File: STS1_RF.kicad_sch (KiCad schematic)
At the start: 84 parts, among them J1 UHF, Q1 SQ2318, Q3 SQ2318, Q4 SQ2318, U10 TQP3M9036, U11 NL17SV04XV5T2G, U16 F2972, U2 LP2985-1.8, U30 TMP36xS, U4 74LVC2G74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

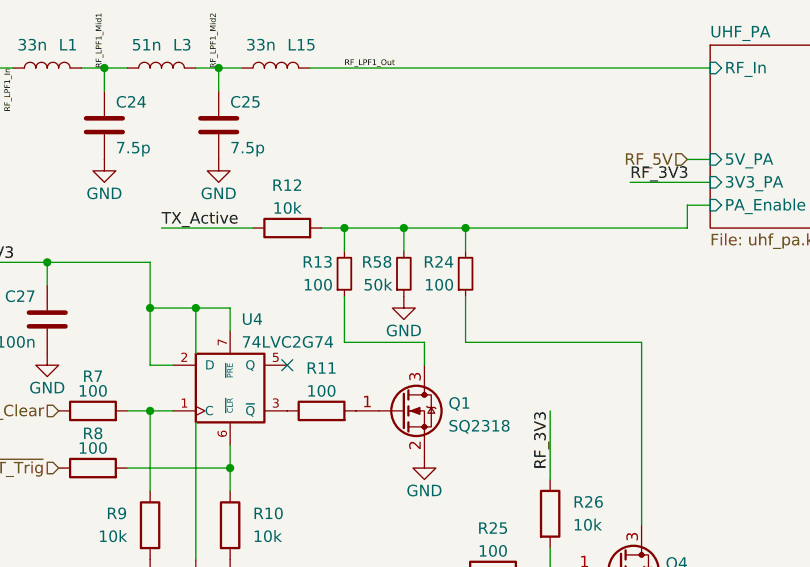
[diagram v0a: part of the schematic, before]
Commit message: Add a pull-up resistor for FLT pin of U12 and decouple U12 and STM with a series resistor
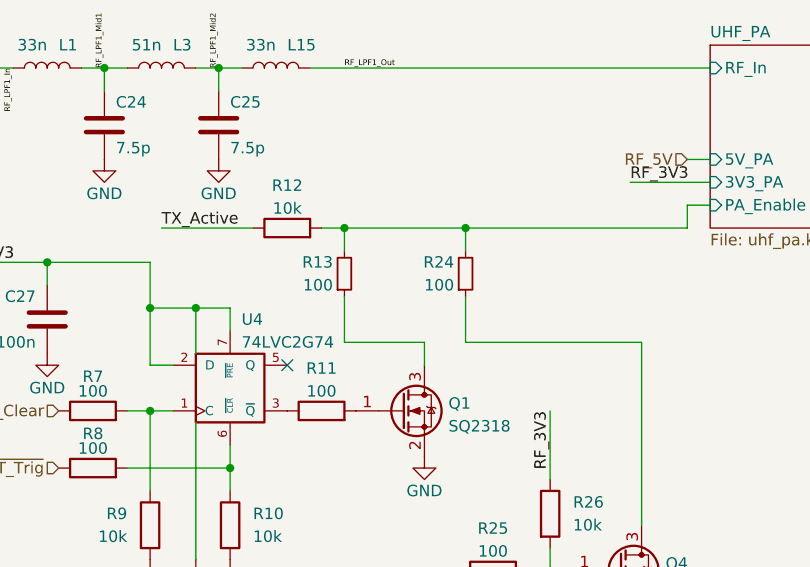
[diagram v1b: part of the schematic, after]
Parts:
- removed R58: 50k, Resistor_SMD:R_0603_1608Metric, symbol Device:R_Small
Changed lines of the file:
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@@
   (junction (at 152.4 50.8) (diameter 0) (color 0 0 0 0)
   )
-  (junction (at 67.564 116.84) (diameter 0) (color 0 0 0 0)
-  )
   (junction (at 48.26 143.51) (diameter 0) (color 0 0 0 0)
   )
@@
     (stroke (width 0) (type default) (color 0 0 0 0))
   )
-  (wire (pts (xy 67.564 116.84) (xy 74.422 116.84))
-    (stroke (width 0) (type default) (color 0 0 0 0))
-  )
   (wire (pts (xy 100.33 55.88) (xy 120.65 55.88))
     (stroke (width 0) (type default) (color 0 0 0 0))
@@
     (stroke (width 0) (type default) (color 0 0 0 0))
   )
-  (wire (pts (xy 67.564 116.84) (xy 67.564 119.38))
-    (stroke (width 0) (type default) (color 0 0 0 0))
-  )
   (wire (pts (xy 165.1 21.59) (xy 172.72 21.59))
     (stroke (width 0) (type default) (color 0 0 0 0))
@@
     (stroke (width 0) (type default) (color 0 0 0 0))
   )
-  (wire (pts (xy 60.96 116.84) (xy 67.564 116.84))
+  (wire (pts (xy 60.96 116.84) (xy 74.422 116.84))
     (stroke (width 0) (type default) (color 0 0 0 0))
   )
@@
     (pin "2")
   )
-  (symbol (lib_id "Device:R_Small") (at 67.564 121.92 0) (mirror x) (unit 1)
-    (in_bom yes) (on_board yes)
-    (property "Reference" "R58" (id 0) (at 66.294 120.65 0)
-      (effects (font (size 1.27 1.27)) (justify right))
-    )
-    (property "Value" "50k" (id 1) (at 66.294 123.19 0)
-      (effects (font (size 1.27 1.27)) (justify right))
-    )
-    (property "Footprint" "Resistor_SMD:R_0603_1608Metric" (id 2) (at 67.564 121.92 0)
-      (effects (font (size 1.27 1.27)) hide)
-    )
-    (property "Datasheet" "~" (id 3) (at 67.564 121.92 0)
-      (effects (font (size 1.27 1.27)) hide)
-    )
-    (property "Description" "" (id 4) (at 67.564 121.92 0)
-      (effects (font (size 1.27 1.27)) hide)
-    )
-    (property "Mnf." "" (id 5) (at 67.564 121.92 0)
-      (effects (font (size 1.27 1.27)) hide)
-    )
-    (property "PartNumber" "" (id 6) (at 67.564 121.92 0)
-      (effects (font (size 1.27 1.27)) hide)
-    )
-    (pin "1")
-    (pin "2")
-  )
   (symbol (lib_id "power:GND") (at 227.33 146.05 0) (unit 1)
     (in_bom yes) (on_board yes)
@@
     (pin "2")
   )
-  (symbol (lib_id "power:GND") (at 67.564 124.46 0) (unit 1)
-    (in_bom yes) (on_board yes)
-    (property "Reference" "#PWR058" (id 0) (at 67.564 130.81 0)
-      (effects (font (size 1.27 1.27)) hide)
-    )
-    (property "Value" "GND" (id 1) (at 67.564 128.27 0))
-    (property "Footprint" "" (id 2) (at 67.564 124.46 0)
-      (effects (font (size 1.27 1.27)) hide)
-    )
-    (property "Datasheet" "" (id 3) (at 67.564 124.46 0)
-      (effects (font (size 1.27 1.27)) hide)
-    )
-    (pin "1")
-  )
   (symbol (lib_id "power:GND") (at 27.94 130.81 0) (unit 1)

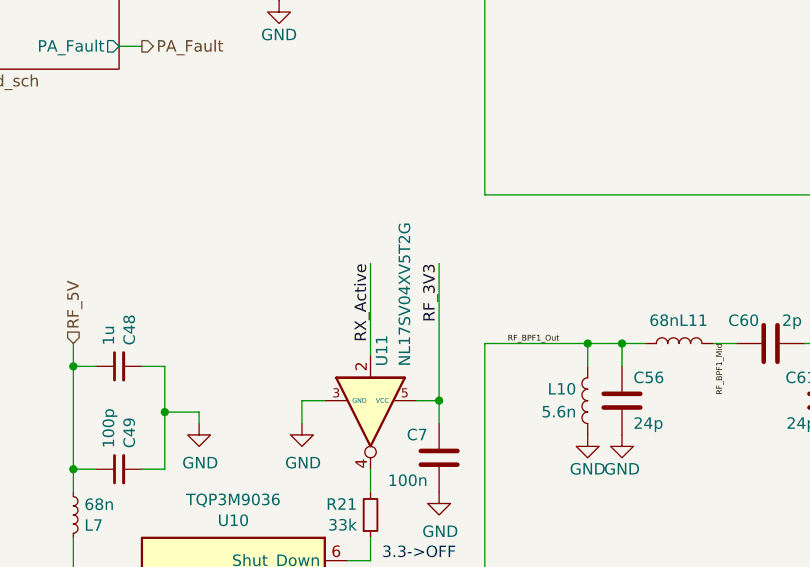
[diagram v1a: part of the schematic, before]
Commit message: Replace U11 NL17SV04XV5T2G with 74LVC1G14Z-7 and add MFT number for R31
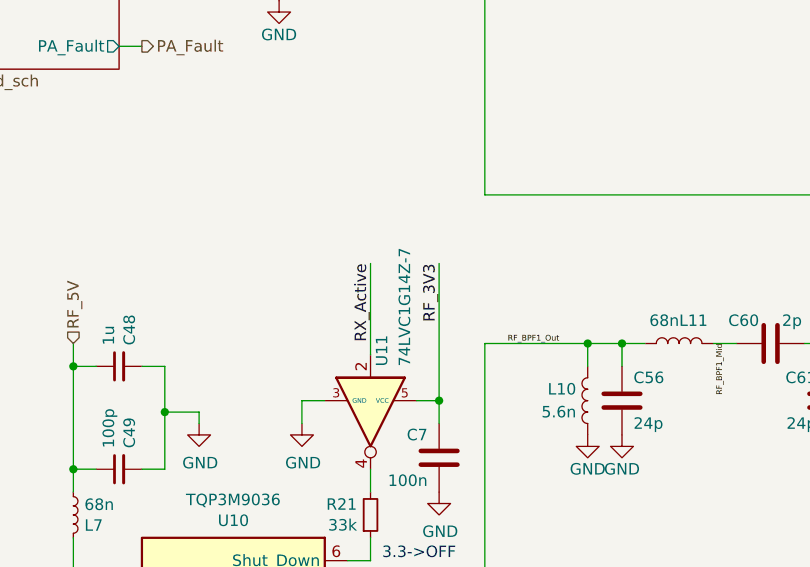
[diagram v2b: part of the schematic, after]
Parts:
- U11: value NL17SV04XV5T2G -> 74LVC1G14Z-7; JLCPCB Part # C185507 -> C3272831; Manufacturer_Part_Number NL17SV04XV5T2G -> 74LVC1G14Z-7
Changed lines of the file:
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@@
       (effects (font (size 1.27 1.27)) (justify right))
     )
-    (property "Value" "NL17SV04XV5T2G" (id 1) (at 161.29 149.86 0)
+    (property "Value" "74LVC1G14Z-7" (id 1) (at 161.29 149.86 0)
       (effects (font (size 1.27 1.27)) (justify right))
     )
@@
       (effects (font (size 1.27 1.27)) hide)
     )
-    (property "Manufacturer_Part_Number" "NL17SV04XV5T2G " (id 6) (at 157.48 153.67 0)
+    (property "Manufacturer_Part_Number" "74LVC1G14Z-7" (id 6) (at 157.48 153.67 0)
       (effects (font (size 1.27 1.27)) hide)
     )
-    (property "JLCPCB Part #" "C185507" (id 7) (at 157.48 153.67 0)
+    (property "JLCPCB Part #" "C3272831" (id 7) (at 157.48 153.67 0)
       (effects (font (size 1.27 1.27)) hide)
     )

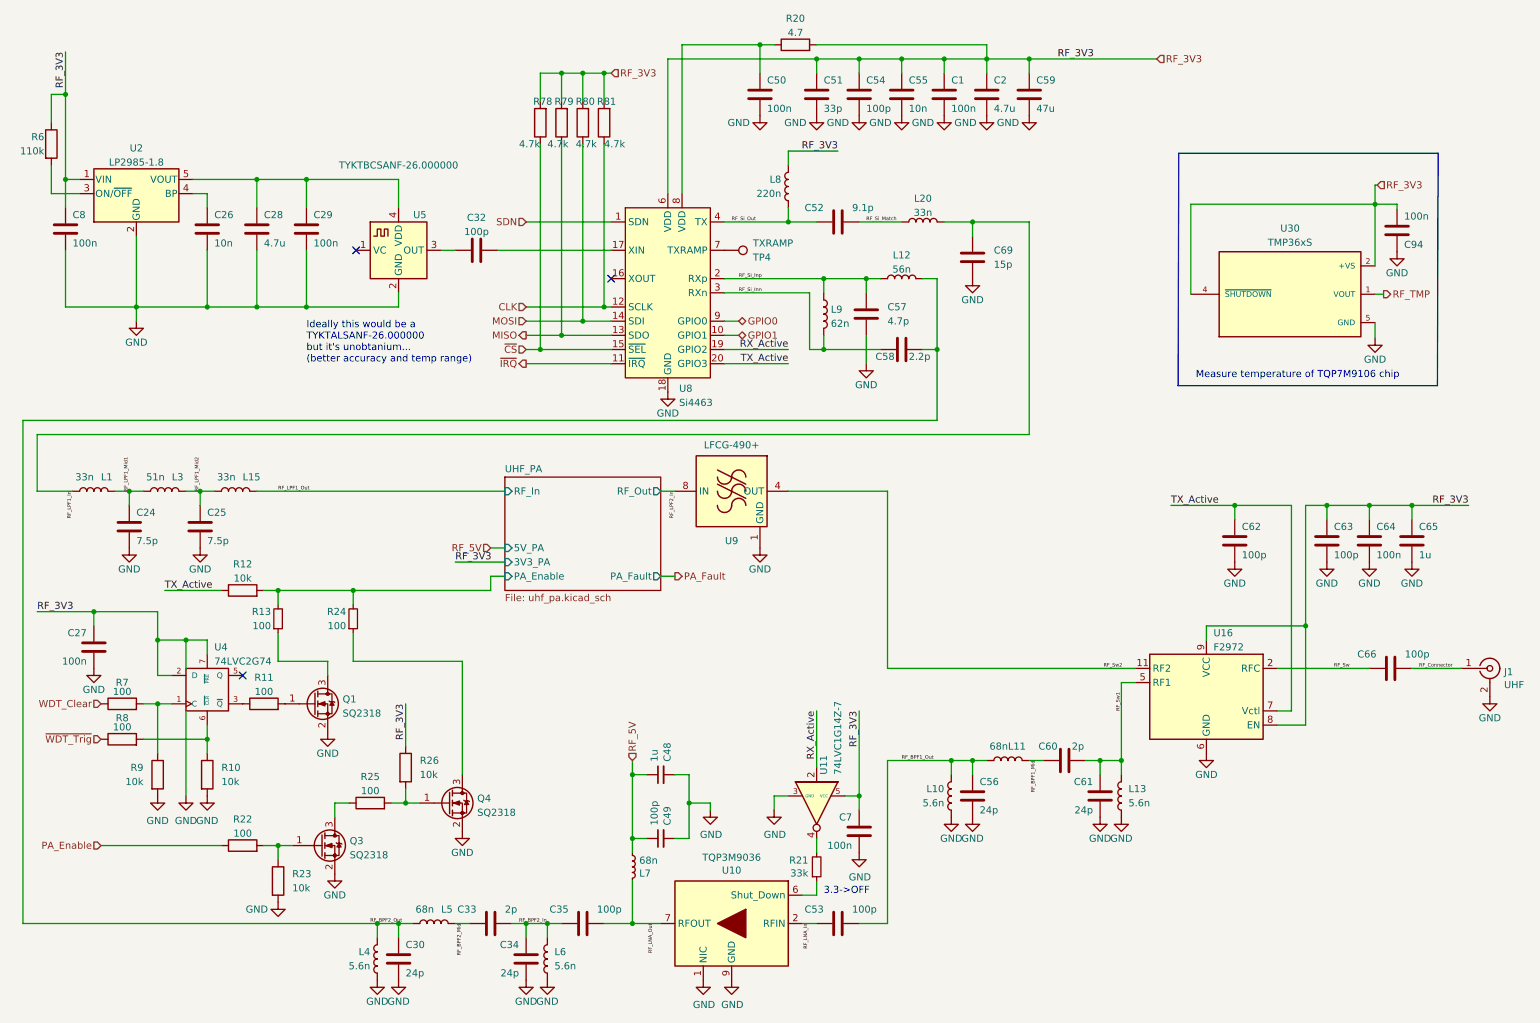
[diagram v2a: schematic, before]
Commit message: Update kicad files to v9.0 from v6.0
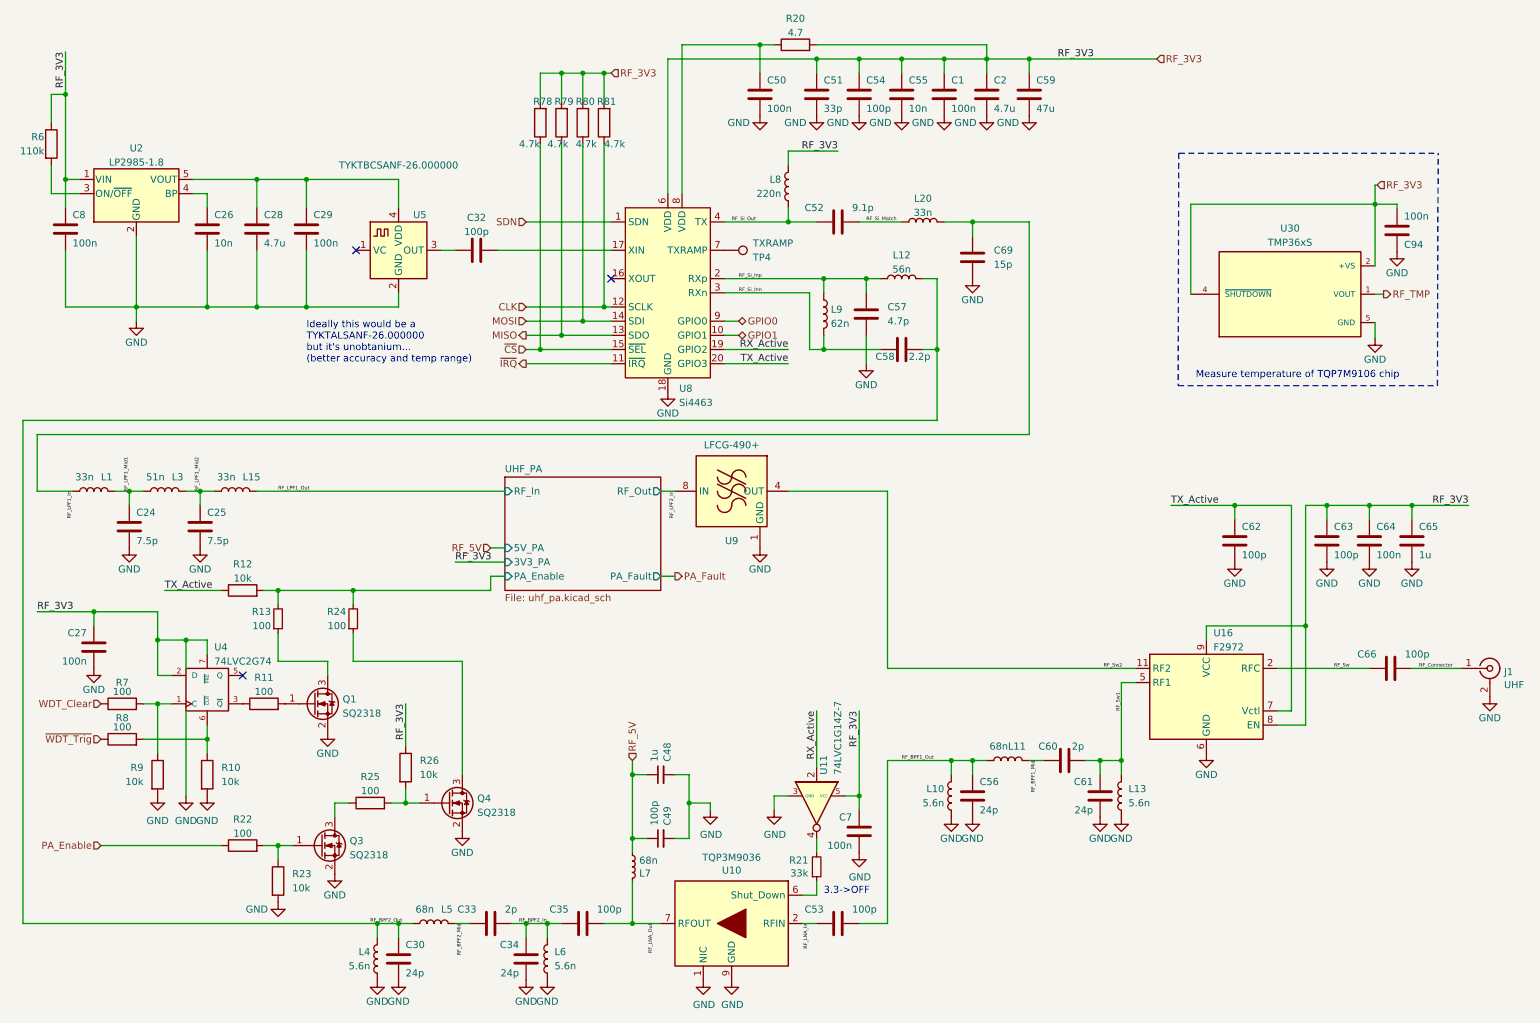
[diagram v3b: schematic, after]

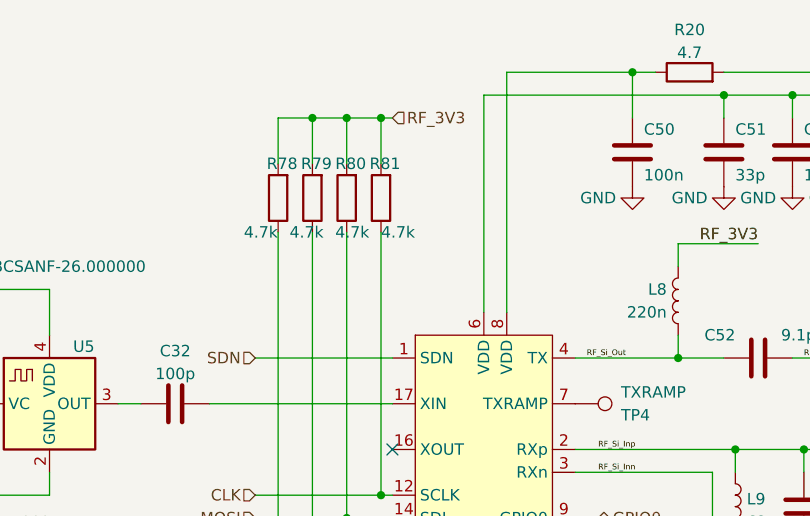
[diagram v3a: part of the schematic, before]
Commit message: Fix the RF-STM SPI communication issue: reduce the value of R81 from 4.7K to 470 Ohm
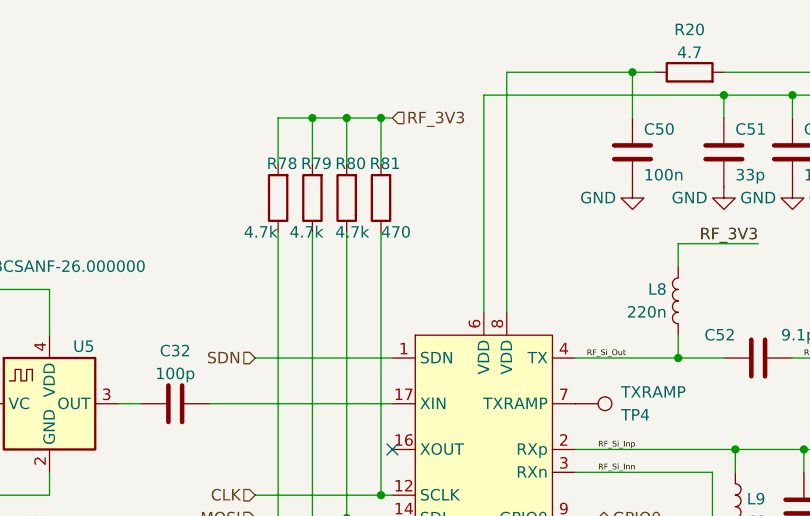
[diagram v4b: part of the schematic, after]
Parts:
- R81: value 4.7k -> 470; JLCPCB Part # C4343266 -> C169259; Manufacturer_Part_Number ERJ-H3EF4701V -> ERJ-3EKF4700V
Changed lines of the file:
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@@
 			)
 		)
-		(property "Description" ""
+		(property "Description" "Voltage Output Temperature Sensors"
 			(at 242.316 63.754 0)
 			(effects
@@
 					(size 1.27 1.27)
 				)
+				(justify bottom)
+				(hide yes)
 			)
 		)
 		(property "MF" "Analog Devices"
 			(at 242.316 87.884 0)
-			(effects
-				(font
-					(size 1.27 1.27)
-				)
-				(justify bottom)
-				(hide yes)
-			)
-		)
-		(property "Description" "Voltage Output Temperature Sensors"
-			(at 242.316 63.754 0)
 			(effects
 				(font
@@
 			)
 		)
-		(property "Value" "4.7k"
+		(property "Value" "470"
 			(at 119.38 36.83 0)
 			(effects
@@
 			)
 		)
-		(property "JLCPCB Part #" "C4343266"
+		(property "JLCPCB Part #" "C169259"
 			(at 119.38 33.02 0)
 			(effects
@@
 			)
 		)
-		(property "Manufacturer_Part_Number" "ERJ-H3EF4701V"
+		(property "Manufacturer_Part_Number" "ERJ-3EKF4700V"
 			(at 119.38 33.02 0)
 			(effects
